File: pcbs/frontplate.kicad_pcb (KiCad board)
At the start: 2 copper layers, 133.3 x 91.7 mm, 5 parts

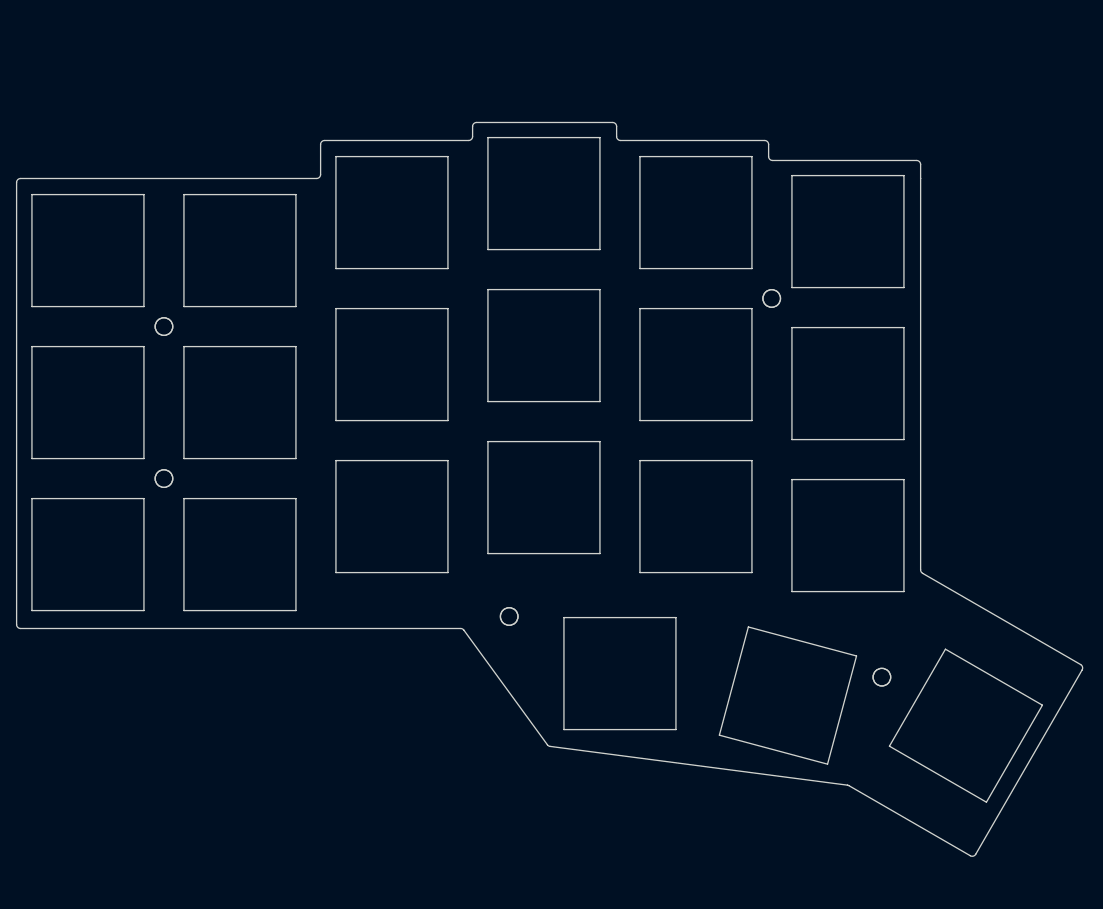
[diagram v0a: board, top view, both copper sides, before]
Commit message: feat: PCB holes alignment
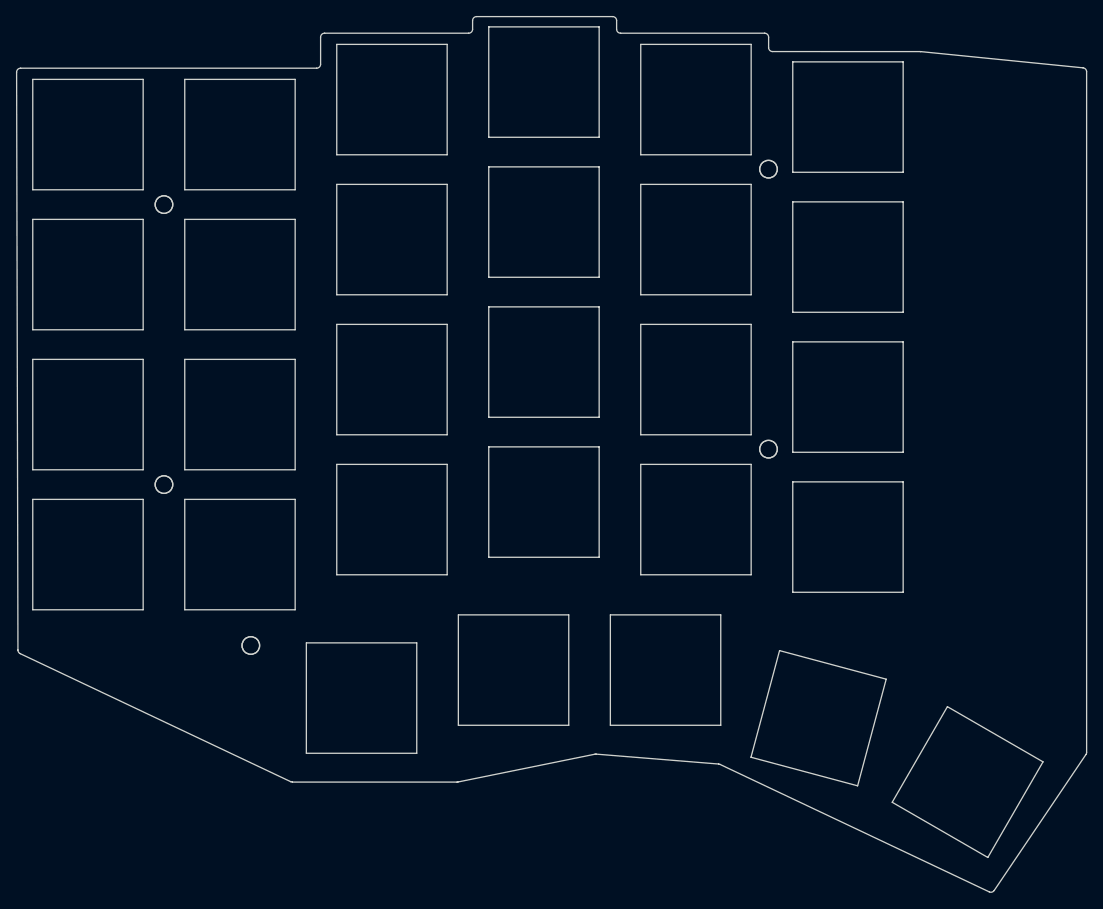
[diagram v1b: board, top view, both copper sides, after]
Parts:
- moved MH5 79.0 mm to (120.4, 111.4), turned to 0 degrees
- moved MH4 38.6 mm to (185.1, 86.8)
- moved MH3 16.2 mm to (185.1, 51.8)
- moved MH1 15.2 mm to (109.5, 56.2)
- moved MH2 0.75 mm to (109.5, 91.2)
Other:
- board size 133.3 x 91.7 mm -> 133.8 x 109.5 mm
